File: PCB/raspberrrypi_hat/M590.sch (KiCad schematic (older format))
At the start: 7 parts, among them J1 SIM_Card

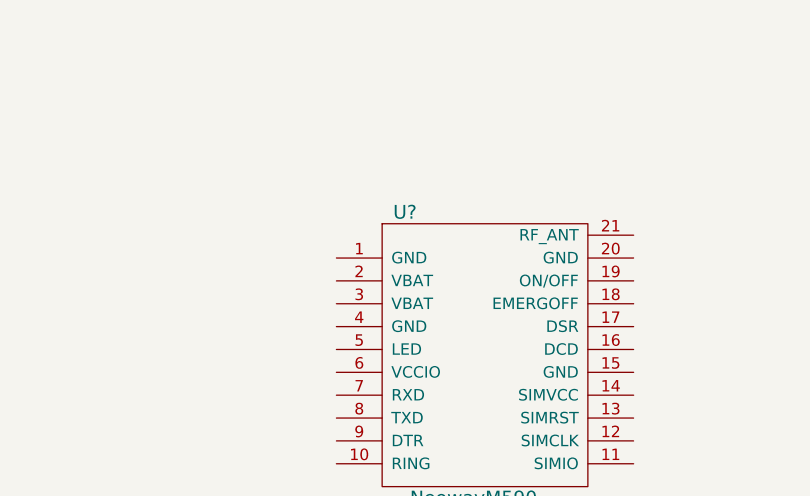
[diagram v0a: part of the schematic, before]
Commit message: Change Pi HAT footprints to SMD 1206_HandSoldering
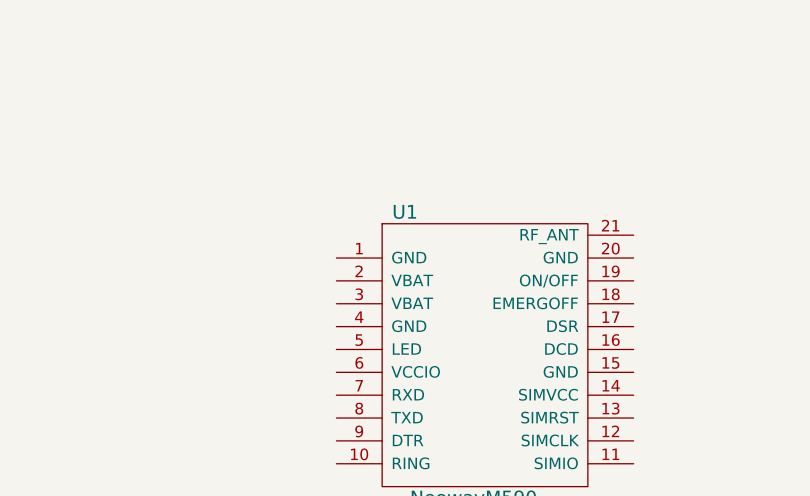
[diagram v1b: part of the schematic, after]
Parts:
- gave numbers to parts that had none: 1
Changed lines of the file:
@@
 	9300 3200 9300 3350
 $Comp
-L NeowayM590 U?
+L NeowayM590 U1
 U 1 1 59519A1D
 P 5050 2900
-F 0 "U?" H 5150 2950 60  0000 C CNN
+F 0 "U1" H 5150 2950 60  0000 C CNN
 F 1 "NeowayM590" H 5450 1700 60  0000 C CNN
 F 2 "" H 5050 2900 60  0001 C CNN

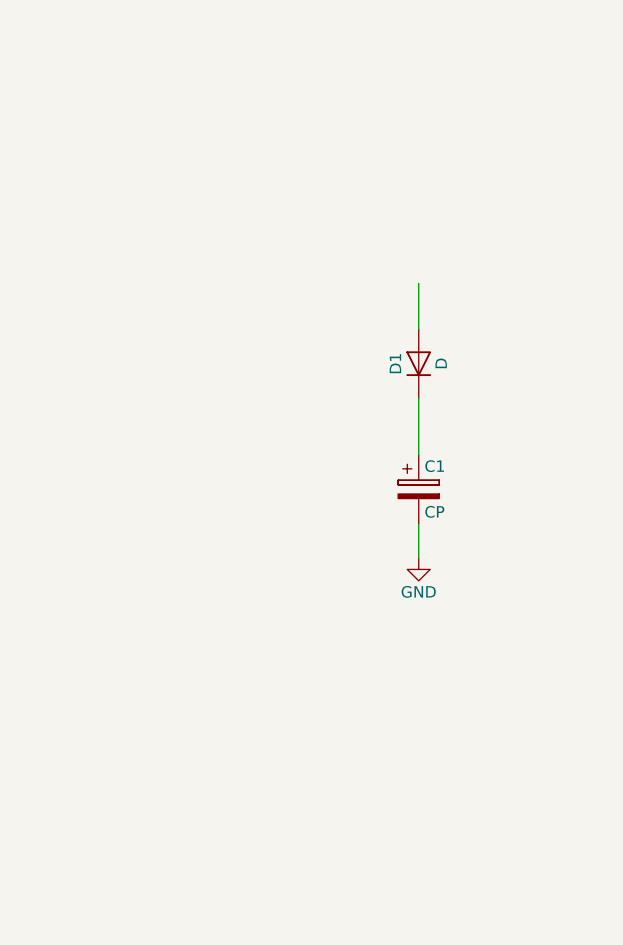
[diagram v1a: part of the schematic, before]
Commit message: Connect hierarchical sheets
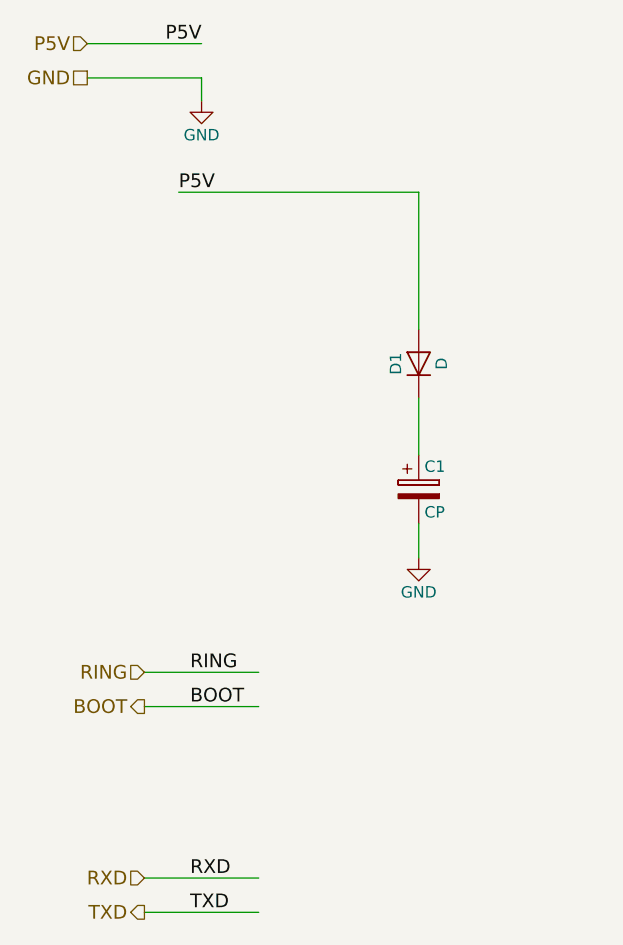
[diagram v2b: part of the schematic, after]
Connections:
- net labels added: BOOT, P5V, RING, RXD, TXD
- wire segments 5 -> 13
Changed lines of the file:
@@
 	2600 2500 2600 2750
 Wire Wire Line
-	2600 2200 2600 2000
+	2600 1600 2600 2200
 $Comp
-L GND #PWR6
+L GND #PWR07
 U 1 1 595187AA
 P 2600 3200
-F 0 "#PWR6" H 2600 2950 50  0001 C CNN
+F 0 "#PWR07" H 2600 2950 50  0001 C CNN
 F 1 "GND" H 2600 3050 50  0000 C CNN
 F 2 "" H 2600 3200 50  0001 C CNN
@@
 $EndComp
 $Comp
-L GND #PWR7
+L GND #PWR08
 U 1 1 595187F4
 P 9300 3350
-F 0 "#PWR7" H 9300 3100 50  0001 C CNN
+F 0 "#PWR08" H 9300 3100 50  0001 C CNN
 F 1 "GND" H 9300 3200 50  0000 C CNN
 F 2 "" H 9300 3350 50  0001 C CNN
@@
 	1    0    0    -1
 $EndComp
+Text Label 1550 1600 0    60   ~ 0
+P5V
+Wire Wire Line
+	1550 1600 2600 1600
+Wire Wire Line
+	1150 950  1650 950
+Wire Wire Line
+	1650 1100 1150 1100
+Text HLabel 1150 1100 0    60   UnSpc ~ 0
+GND
+Text HLabel 1150 950  0    60   Input ~ 0
+P5V
+Text Label 1650 950  2    60   ~ 0
+P5V
+$Comp
+L GND #PWR09
+U 1 1 5952C140
+P 1650 1200
+F 0 "#PWR09" H 1650 950 50  0001 C CNN
+F 1 "GND" H 1650 1050 50  0000 C CNN
+F 2 "" H 1650 1200 50  0001 C CNN
+F 3 "" H 1650 1200 50  0001 C CNN
+	1    1650 1200
+	1    0    0    -1
+$EndComp
+Wire Wire Line
+	1650 1100 1650 1200
+Wire Wire Line
+	1400 3850 1900 3850
+Wire Wire Line
+	1900 3700 1400 3700
+Text HLabel 1400 3700 0    60   Input ~ 0
+RING
+Text HLabel 1400 3850 0    60   Output ~ 0
+BOOT
+Wire Wire Line
+	1400 4750 1900 4750
+Wire Wire Line
+	1900 4600 1400 4600
+Text HLabel 1400 4600 0    60   Input ~ 0
+RXD
+Text HLabel 1400 4750 0    60   Output ~ 0
+TXD
+Text Label 1600 3700 0    60   ~ 0
+RING
+Text Label 1600 3850 0    60   ~ 0
+BOOT
+Text Label 1600 4600 0    60   ~ 0
+RXD
+Text Label 1600 4750 0    60   ~ 0
+TXD
 $EndSCHEMATC

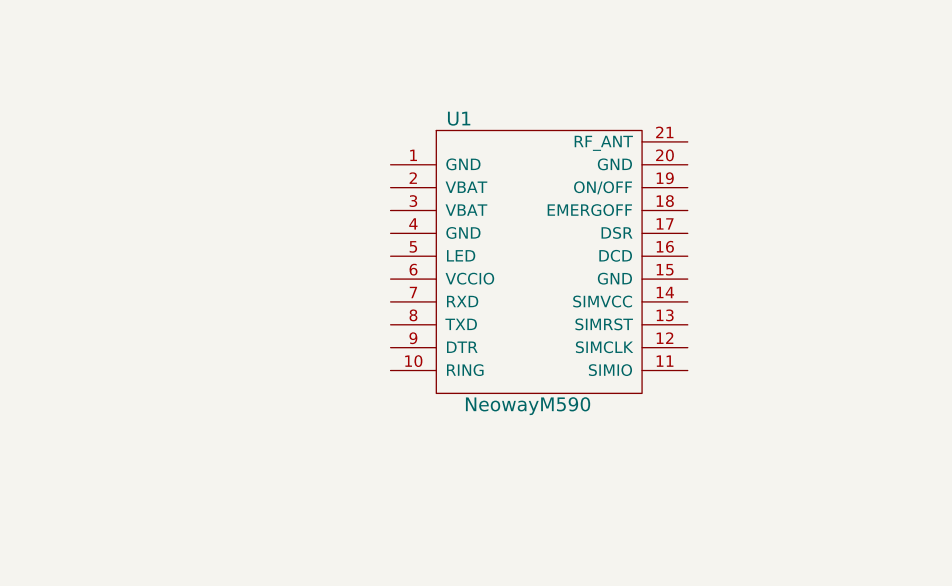
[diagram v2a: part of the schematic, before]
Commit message: Create NeowayM590 footprint
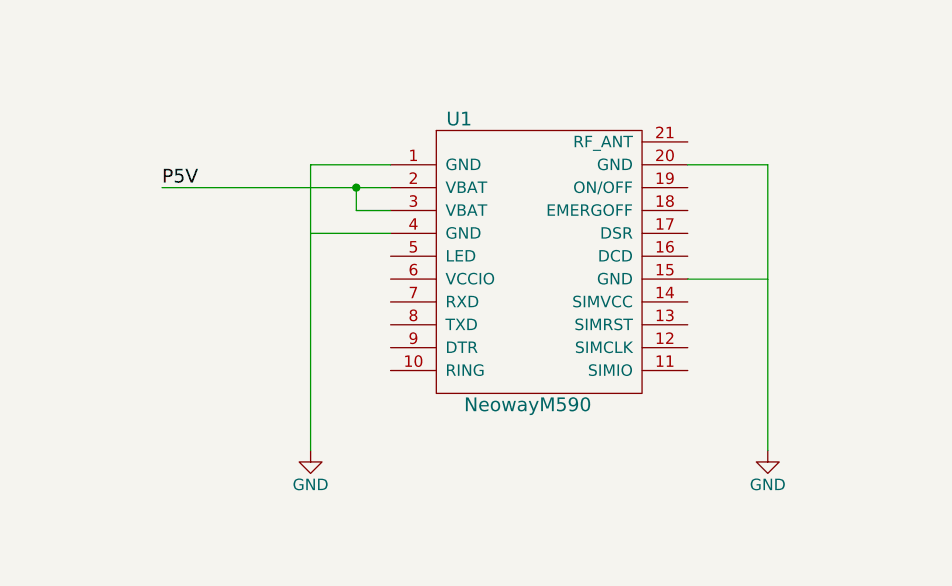
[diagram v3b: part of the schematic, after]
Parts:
- U1: footprint (none) -> project_footprints:NeowayM590
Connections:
- wire segments 13 -> 22
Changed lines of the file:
@@
 F 0 "U1" H 5150 2950 60  0000 C CNN
 F 1 "NeowayM590" H 5450 1700 60  0000 C CNN
-F 2 "" H 5050 2900 60  0001 C CNN
+F 2 "project_footprints:NeowayM590" H 5050 2900 60  0001 C CNN
 F 3 "" H 5050 2900 60  0001 C CNN
 	1    5050 2900
@@
 Text Label 1600 4750 0    60   ~ 0
 TXD
+Wire Wire Line
+	6150 3050 6500 3050
+Wire Wire Line
+	6150 3550 6500 3550
+Wire Wire Line
+	4500 3050 4850 3050
+Wire Wire Line
+	4500 3350 4850 3350
+Wire Wire Line
+	4500 3050 4500 4300
+Wire Wire Line
+	6500 3050 6500 4300
+$Comp
+L GND #PWR?
+U 1 1 5952C301
+P 6500 4300
+F 0 "#PWR?" H 6500 4050 50  0001 C CNN
+F 1 "GND" H 6500 4150 50  0000 C CNN
+F 2 "" H 6500 4300 50  0001 C CNN
+F 3 "" H 6500 4300 50  0001 C CNN
+	1    6500 4300
+	1    0    0    -1
+$EndComp
+$Comp
+L GND #PWR?
+U 1 1 5952C323
+P 4500 4300
+F 0 "#PWR?" H 4500 4050 50  0001 C CNN
+F 1 "GND" H 4500 4150 50  0000 C CNN
+F 2 "" H 4500 4300 50  0001 C CNN
+F 3 "" H 4500 4300 50  0001 C CNN
+	1    4500 4300
+	1    0    0    -1
+$EndComp
+Wire Wire Line
+	4850 3150 3850 3150
+Wire Wire Line
+	4850 3250 4700 3250
+Wire Wire Line
+	4700 3250 4700 3150
+Connection ~ 4700 3150
+Text Label 3850 3150 0    60   ~ 0
+P5V
 $EndSCHEMATC

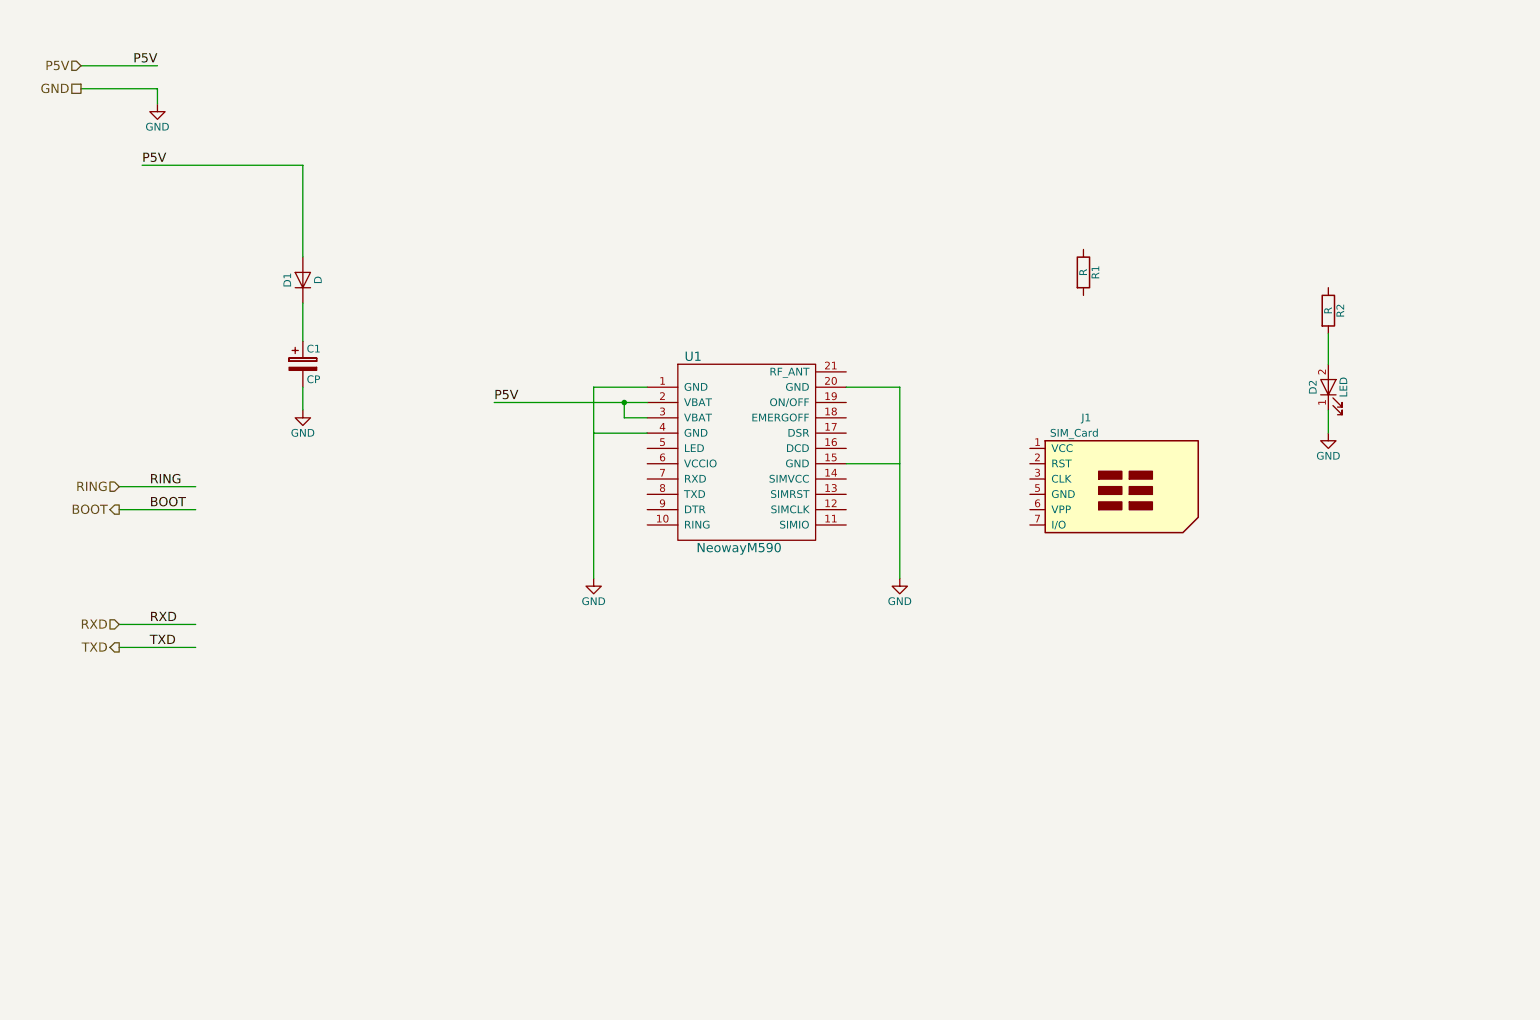
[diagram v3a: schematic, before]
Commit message: SCH: M590 and pi wirering
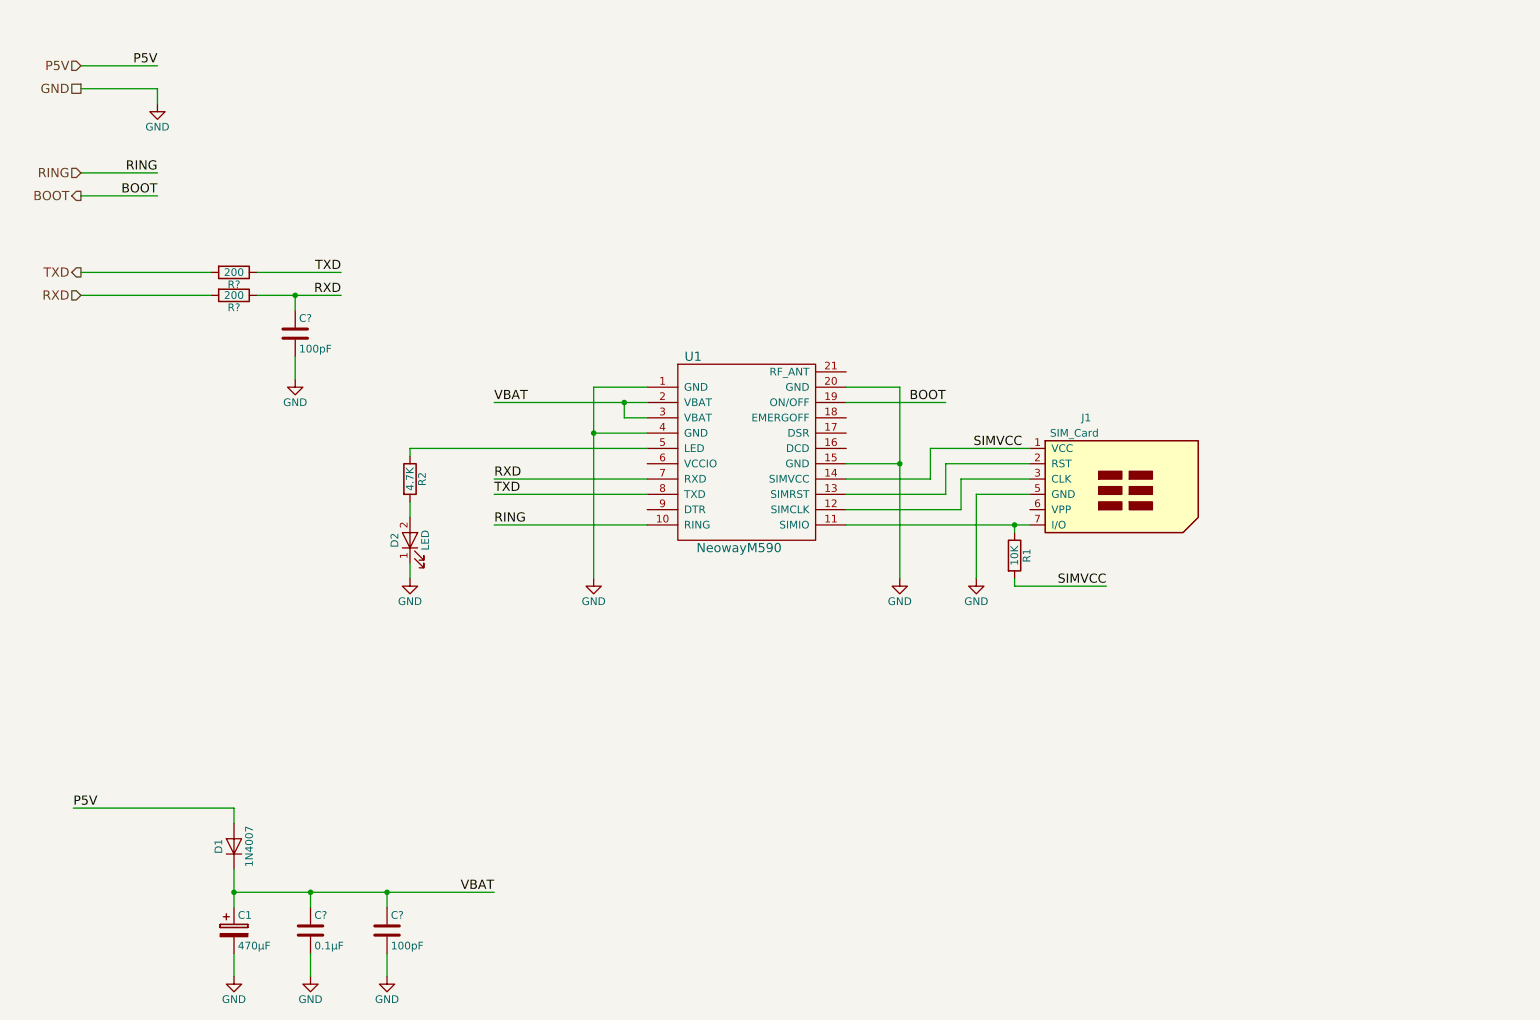
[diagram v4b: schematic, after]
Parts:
- added C?: 0.1µF, symbol C
- added C? (x2): 100pF, symbol C
- added R? (x2): 200, Resistors_SMD:R_1206_HandSoldering, symbol R
- C1: value CP -> 470µF
- D1: value D -> 1N4007
- R1: value R -> 10K
- R2: value R -> 4.7K
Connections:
- net labels added: SIMVCC, VBAT
- wire segments 22 -> 52
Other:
- moved on the sheet: C1, D1, D2, R1, R2

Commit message: SCH: Change page size to A4, update footer and add comments about parts
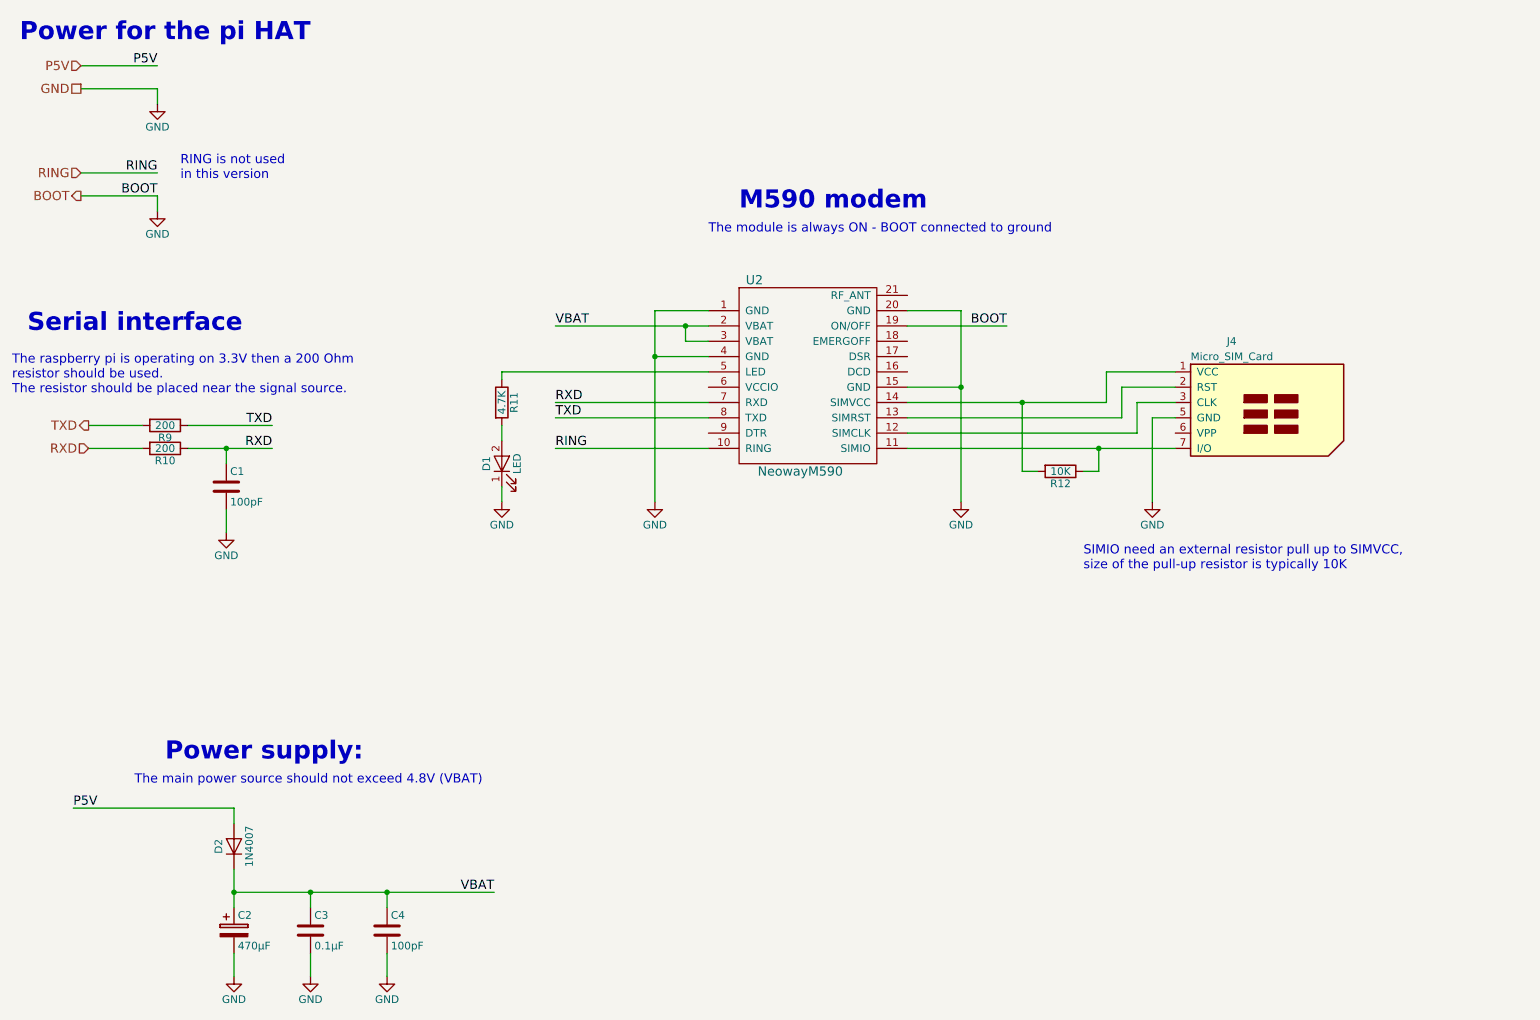
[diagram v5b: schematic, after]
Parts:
- J4: renamed from J1; value SIM_Card -> Micro_SIM_Card
- gave numbers to parts that had none: 5
- renumbered C1 to C2, D2 to D1, D1 to D2, R2 to R11, R1 to R12, U1 to U2
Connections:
- net BOOT is gone; now on net GND: U2.19 (ON/OFF)
- net SIMVCC: no longer names the net of J4.1 (VCC), R12.2, U2.14 (SIMVCC)
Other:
- note added: "M590 modem"
- note added: "Power for the pi HAT"
- note added: "Power supply:"
- note added: "RING is not used\nin this version"
- note added: "SIMIO need an external resistor pull up to SIMVCC,\nsize of the pull-up resistor is typically 10K"
- note added: "Serial interface"
- note added: "The main power source should not exceed 4.8V (VBAT)"
- note added: "The module is always ON - BOOT connected to ground"
- note added: "The raspberry pi is operating on 3.3V then a 200 Ohm\nresistor should be used.\nThe resistor should be placed near the signal source."
- moved on the sheet: C1, D1, J4, R10, R11, R12, R9, U2
